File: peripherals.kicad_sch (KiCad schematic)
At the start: 47 parts, among them J10 532611071, J11 ERF8-020-05.0-S-DV-L-TR, J8 TC2050-IDC-NL, J9 533980471, Q4 PJE138K, Q5 PJE138K, U20 NTS0102GT, U21 ICM-20602

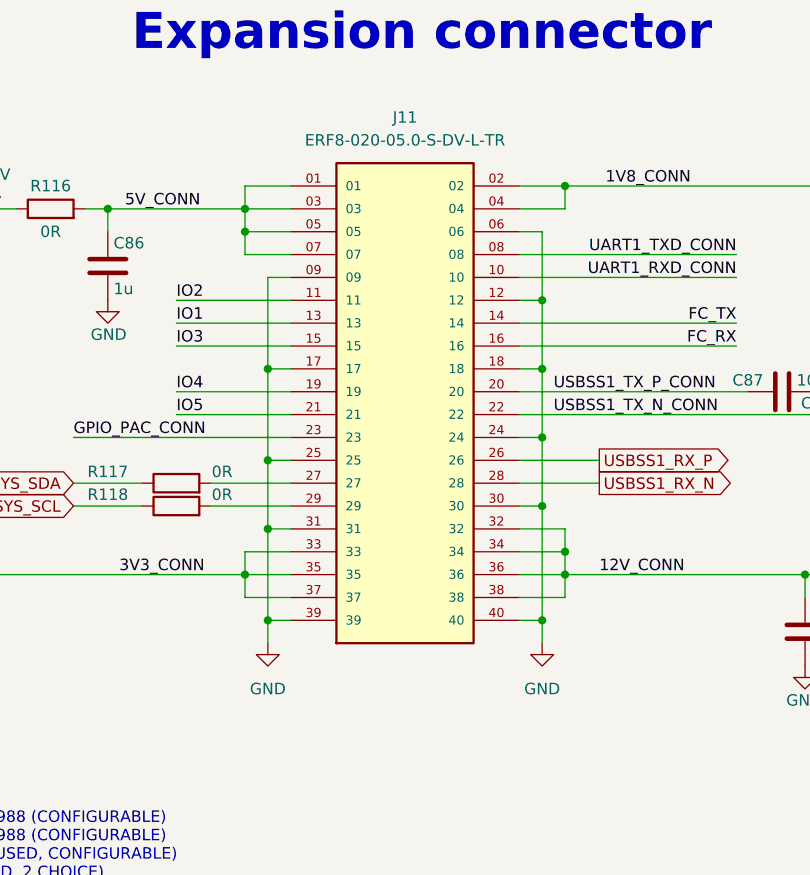
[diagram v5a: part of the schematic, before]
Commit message: Footprints well assigned, XT30 added, Shields grounded
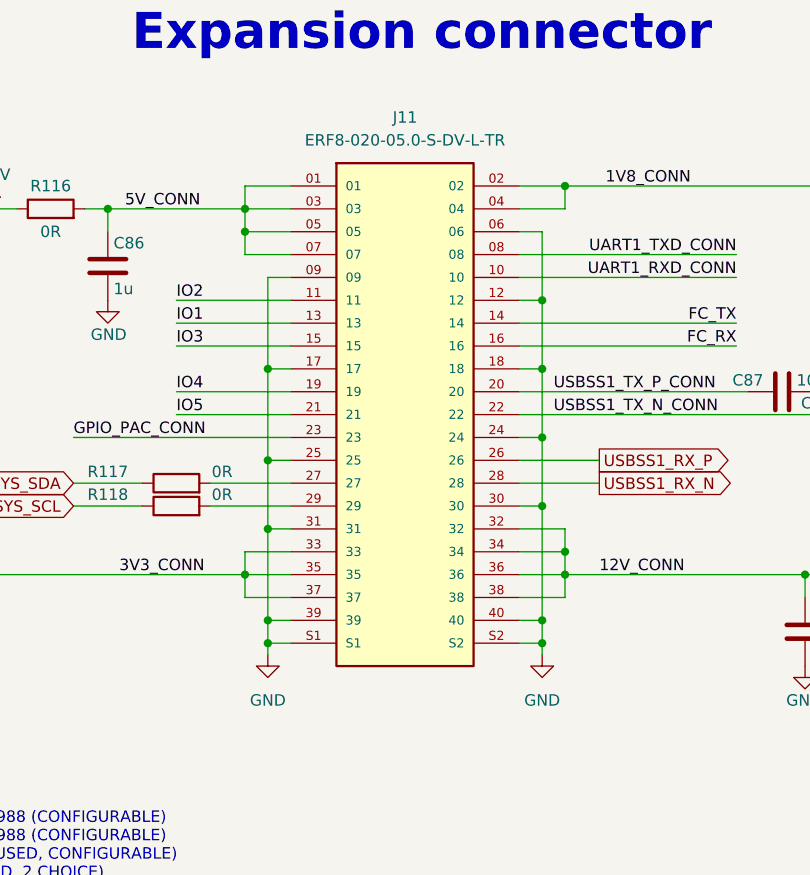
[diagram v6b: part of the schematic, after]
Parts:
- J11: footprint jetson-orin-baseboard-footprints:ERF8-040-XX.X-X-DV-XX -> jetson-orin-baseboard-footprints:SAMTEC_ERF8-020-05.0-S-DV-L-TR
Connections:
- net GND: now also J11.S1, J11.S2
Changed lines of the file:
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@@
   (junction (at 396.24 124.46) (diameter 0) (color 0 0 0 0)
   )
+  (junction (at 335.28 91.44) (diameter 0) (color 0 0 0 0)
+  )
   (junction (at 26.67 173.99) (diameter 0) (color 0 0 0 0)
   )
@@
   (junction (at 335.28 88.9) (diameter 0) (color 0 0 0 0)
   )
+  (junction (at 304.8 91.44) (diameter 0) (color 0 0 0 0)
+  )
   (junction (at 175.26 92.71) (diameter 0) (color 0 0 0 0)
   )
@@
     (stroke (width 0) (type default))
   )
+  (wire (pts (xy 304.8 88.9) (xy 304.8 91.44))
+    (stroke (width 0) (type default))
+  )
   (wire (pts (xy 175.26 266.7) (xy 184.15 266.7))
     (stroke (width 0) (type default))
@@
     (stroke (width 0) (type default))
   )
+  (wire (pts (xy 304.8 91.44) (xy 307.34 91.44))
+    (stroke (width 0) (type default))
+  )
   (wire (pts (xy 63.5 54.61) (xy 69.85 54.61))
     (stroke (width 0) (type default))
@@
     (stroke (width 0) (type default))
   )
+  (wire (pts (xy 332.74 91.44) (xy 335.28 91.44))
+    (stroke (width 0) (type default))
+  )
   (wire (pts (xy 165.1 162.56) (xy 191.77 162.56))
     (stroke (width 0) (type default))
@@
     (stroke (width 0) (type default))
   )
-  (wire (pts (xy 304.8 88.9) (xy 304.8 91.44))
+  (wire (pts (xy 335.28 91.44) (xy 335.28 92.71))
     (stroke (width 0) (type default))
   )
@@
     (stroke (width 0) (type default))
   )
+  (wire (pts (xy 304.8 91.44) (xy 304.8 92.71))
+    (stroke (width 0) (type default))
+  )
   (wire (pts (xy 392.43 144.78) (xy 396.24 144.78))
     (stroke (width 0) (type default))
@@
     )
   )
-  (symbol (lib_id "jetson-orin-baseboard:GND") (at 304.8 91.44 0) (unit 1)
+  (symbol (lib_id "jetson-orin-baseboard:GND") (at 304.8 92.71 0) (unit 1)
     (in_bom yes) (on_board yes) (dnp no) (fields_autoplaced)
-    (property "Reference" "#PWR0196" (at 304.8 97.79 0)
+    (property "Reference" "#PWR0196" (at 304.8 99.06 0)
       (effects (font (size 1.27 1.27)) hide)
     )
-    (property "Value" "GND" (at 304.8 96.52 0)
+    (property "Value" "GND" (at 304.8 97.79 0)
       (effects (font (size 1.27 1.27)))
     )
-    (property "Footprint" "" (at 304.8 91.44 0)
+    (property "Footprint" "" (at 304.8 92.71 0)
       (effects (font (size 1.27 1.27)) hide)
     )
-    (property "Datasheet" "" (at 304.8 91.44 0)
+    (property "Datasheet" "" (at 304.8 92.71 0)
       (effects (font (size 1.27 1.27)) hide)
     )
@@
     )
   )
-  (symbol (lib_id "jetson-orin-baseboard:GND") (at 335.28 91.44 0) (unit 1)
+  (symbol (lib_id "jetson-orin-baseboard:GND") (at 335.28 92.71 0) (unit 1)
     (in_bom yes) (on_board yes) (dnp no) (fields_autoplaced)
-    (property "Reference" "#PWR0180" (at 335.28 97.79 0)
+    (property "Reference" "#PWR0180" (at 335.28 99.06 0)
       (effects (font (size 1.27 1.27)) hide)
     )
-    (property "Value" "GND" (at 335.28 96.52 0)
+    (property "Value" "GND" (at 335.28 97.79 0)
       (effects (font (size 1.27 1.27)))
     )
-    (property "Footprint" "" (at 335.28 91.44 0)
+    (property "Footprint" "" (at 335.28 92.71 0)
       (effects (font (size 1.27 1.27)) hide)
     )
-    (property "Datasheet" "" (at 335.28 91.44 0)
+    (property "Datasheet" "" (at 335.28 92.71 0)
       (effects (font (size 1.27 1.27)) hide)
     )
@@
       (effects (font (size 1.27 1.27)))
     )
-    (property "Footprint" "jetson-orin-baseboard-footprints:ERF8-040-XX.X-X-DV-XX" (at 320.04 66.04 0)
+    (property "Footprint" "jetson-orin-baseboard-footprints:SAMTEC_ERF8-020-05.0-S-DV-L-TR" (at 320.04 66.04 0)
       (effects (font (size 1.27 1.27)) (justify bottom) hide)
     )
@@
     (pin "39")
     (pin "40")
+    (pin "S1")
+    (pin "S2")
     (instances
       (project "jetson-orin-baseboard"

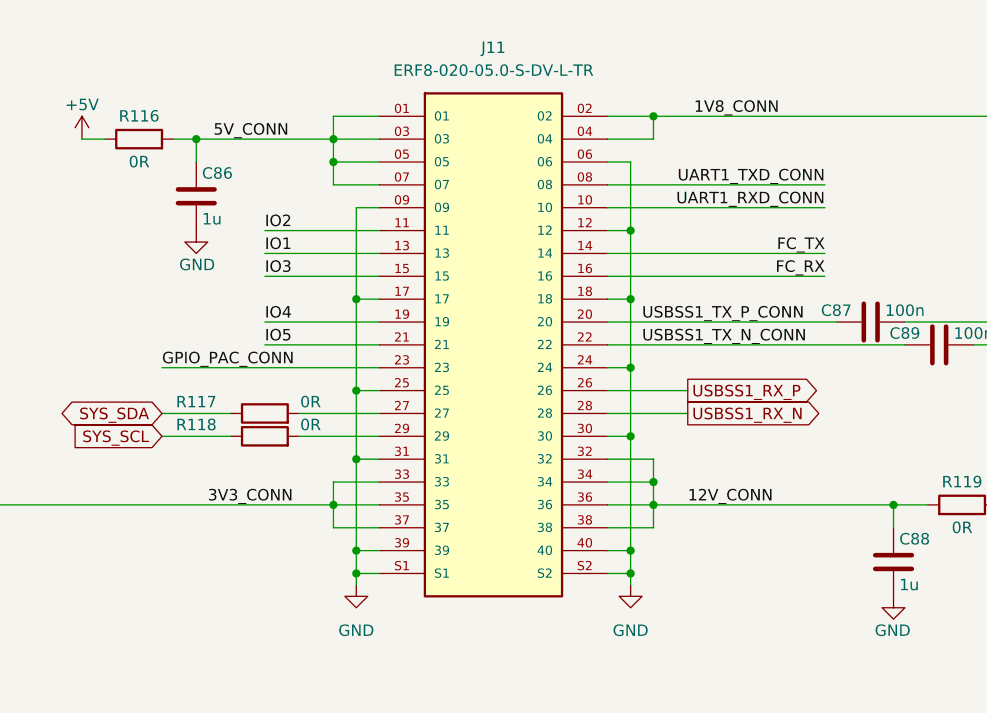
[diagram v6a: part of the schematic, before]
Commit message: Text size changes and positioning important components part 1
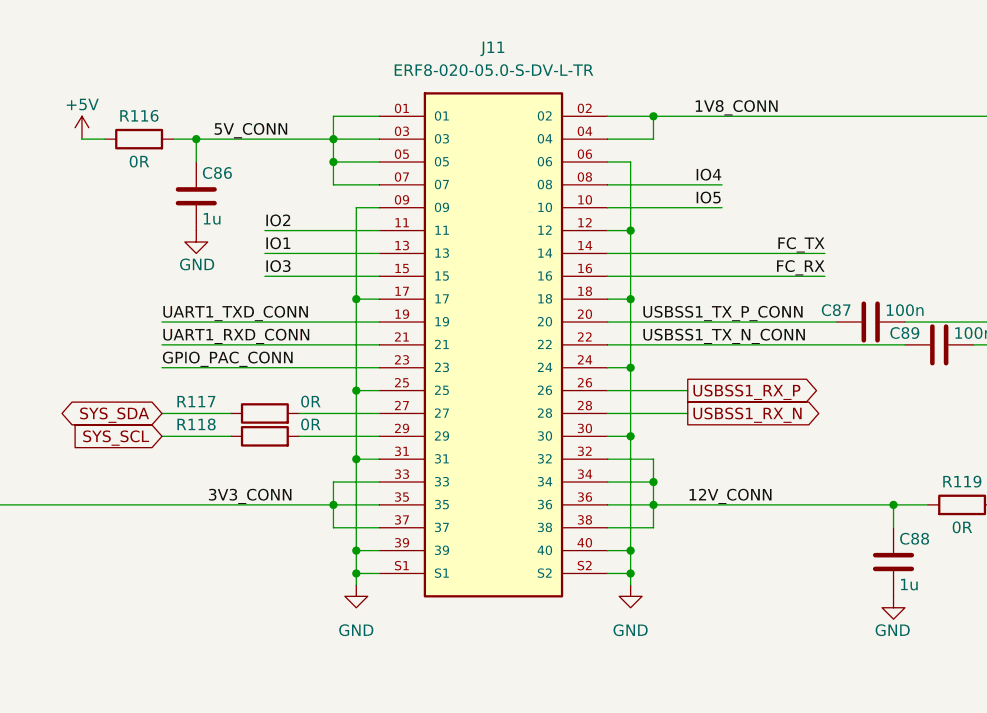
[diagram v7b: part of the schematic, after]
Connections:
- net IO4: now also J11.08; no longer J11.19
- net IO5: now also J11.10; no longer J11.21
- net UART1_RXD_CONN: now also J11.21; no longer J11.10
- net UART1_TXD_CONN: now also J11.19; no longer J11.08
